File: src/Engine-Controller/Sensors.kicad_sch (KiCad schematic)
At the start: 24 parts, among them P10 39299043, P11 39299043, P12 39299043, P13 39299043, P14 39299043, P15 39299043, P8 39299043, P9 39299043, U12 MAX4617EUE+T, U13 MAX4617EUE+T, U7 MC74HC4066ADG, U8 AD623ARZ-R7, U9 MC74HC4066ADG

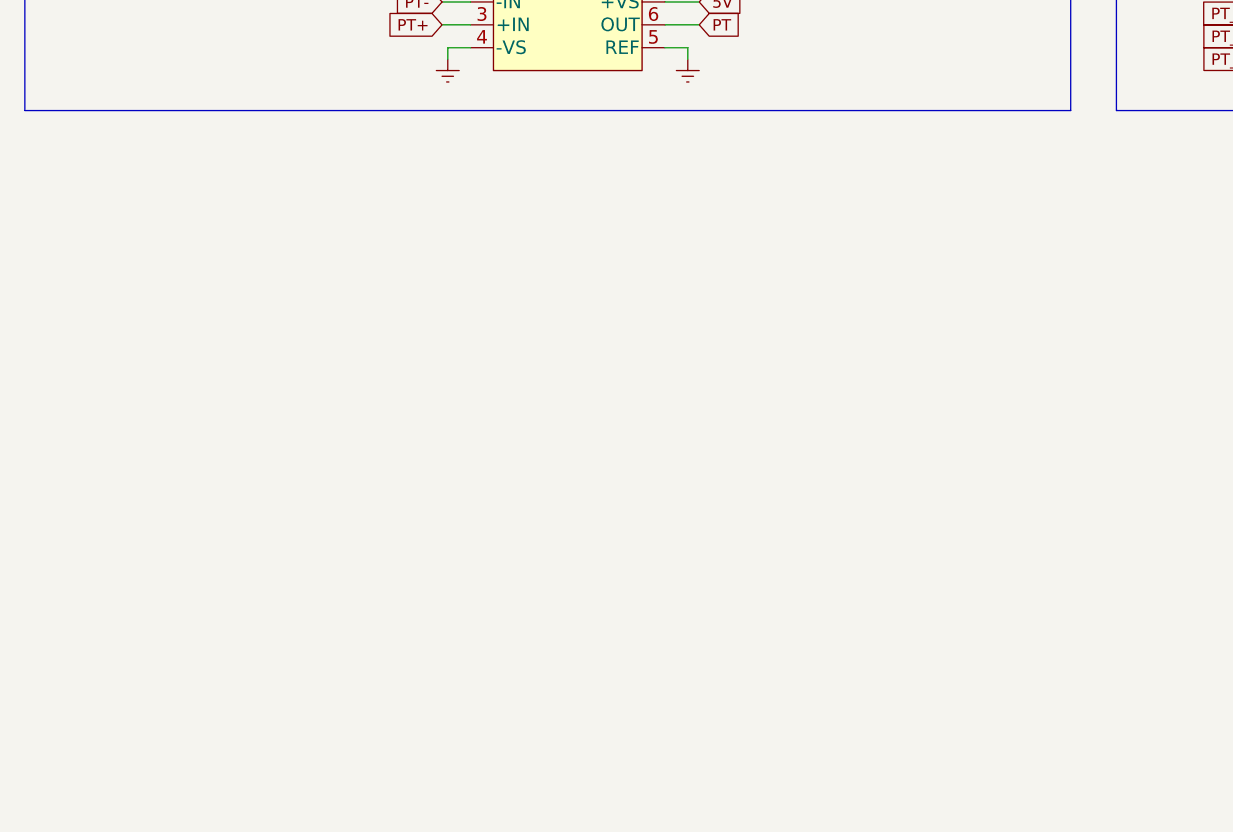
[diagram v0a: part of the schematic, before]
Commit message: added thermocouple IC to schematic
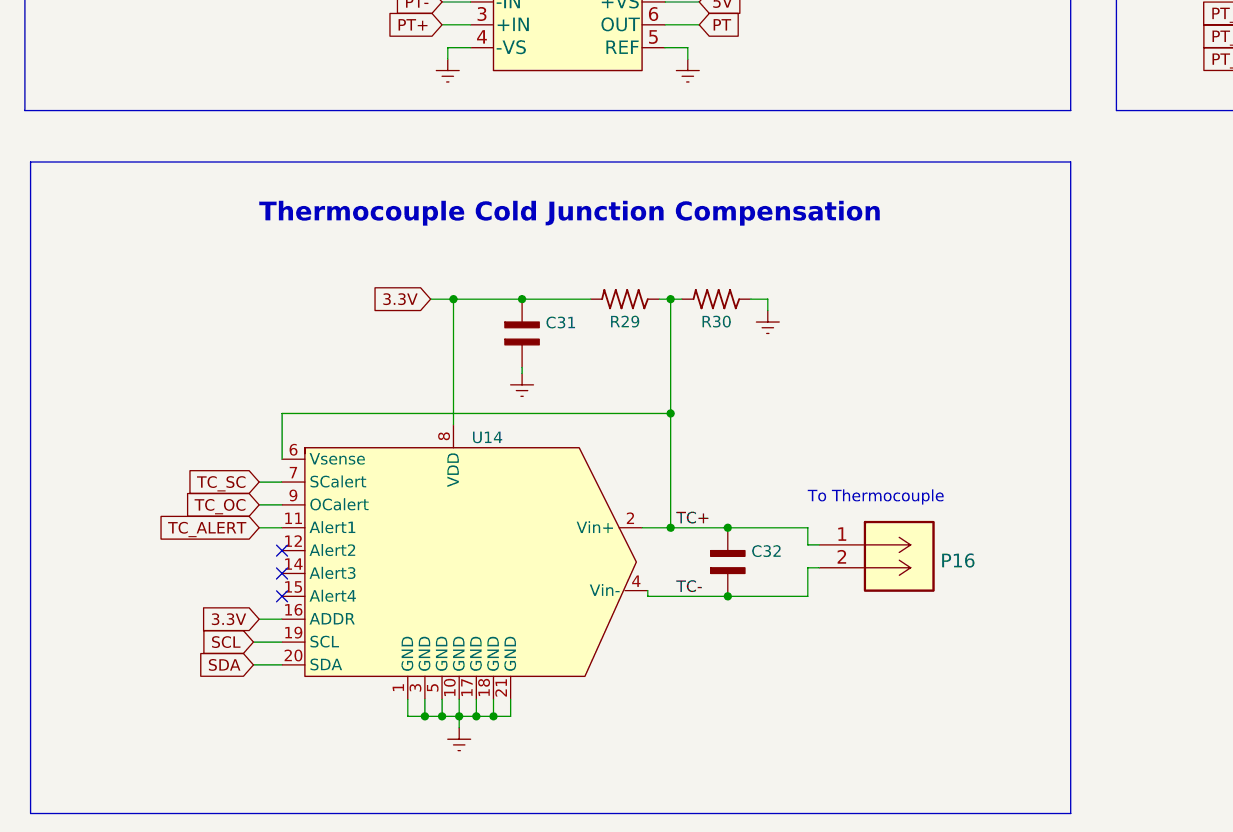
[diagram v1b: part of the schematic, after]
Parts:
- added C31, C32: (no value), symbol Engine-Controller:CAP_0603
- added P16: (no value), symbol Engine-Controller:647676-2
- added R29, R30: (no value), symbol Engine-Controller:RES_0603
- added U14: (no value), symbol Engine-Controller:MCP96L01T-E_MX
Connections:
- net 3.3V: now also C31.2, R29.2, U14.16 (ADDR), U14.8 (VDD)
- net Earth: now also C31.1, R30.1, U14.1 (GND), U14.10 (GND), U14.17 (GND), U14.18 (GND), U14.21 (GND), U14.3 (GND), U14.5 (GND)
- new net SCL: U14.19 (SCL)
- new net SDA: U14.20 (SDA)
- new net TC+: C32.2, P16.1, R29.1, R30.2, U14.2 (Vin+), U14.6 (Vsense)
- new net TC-: C32.1, P16.2, U14.4 (Vin-)
- new net TC_ALERT: U14.11 (Alert1)
- new net TC_OC: U14.9 (OCalert)
- new net TC_SC: U14.7 (SCalert)
- no-connect marks 0 -> 3
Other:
- note added: "Thermocouple Cold Junction Compensation"
- note added: "To Thermocouple"

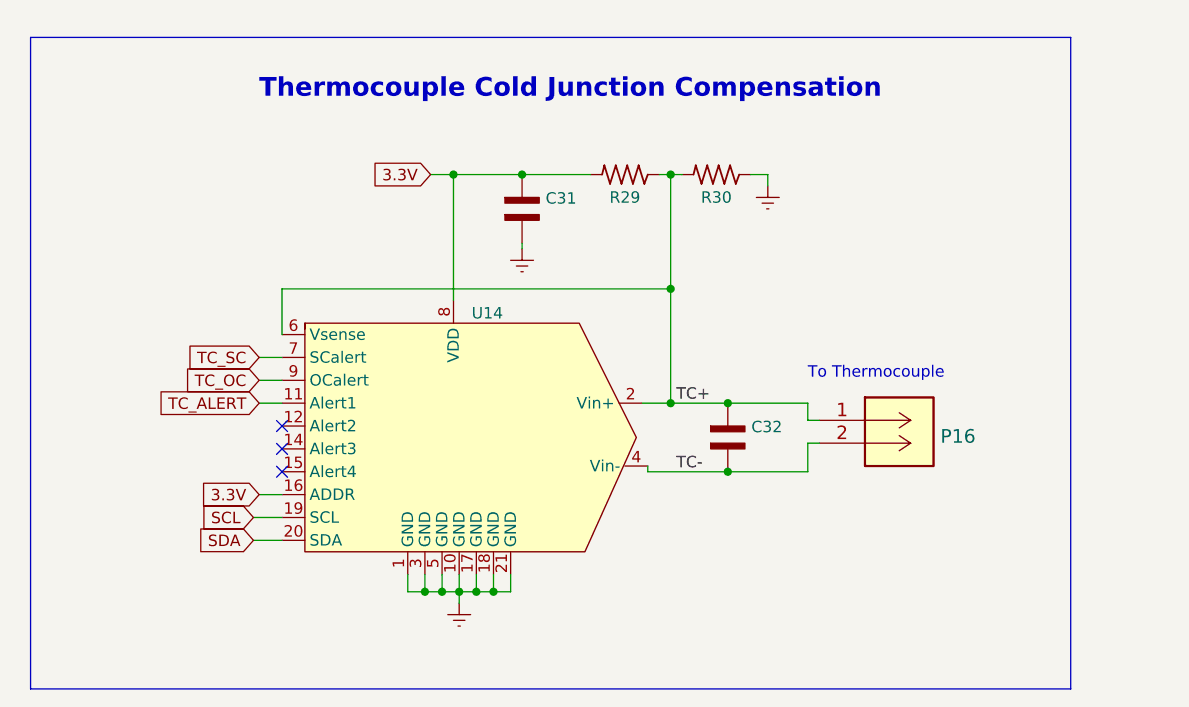
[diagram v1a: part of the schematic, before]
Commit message: added I2C pullups to thermocouple IC
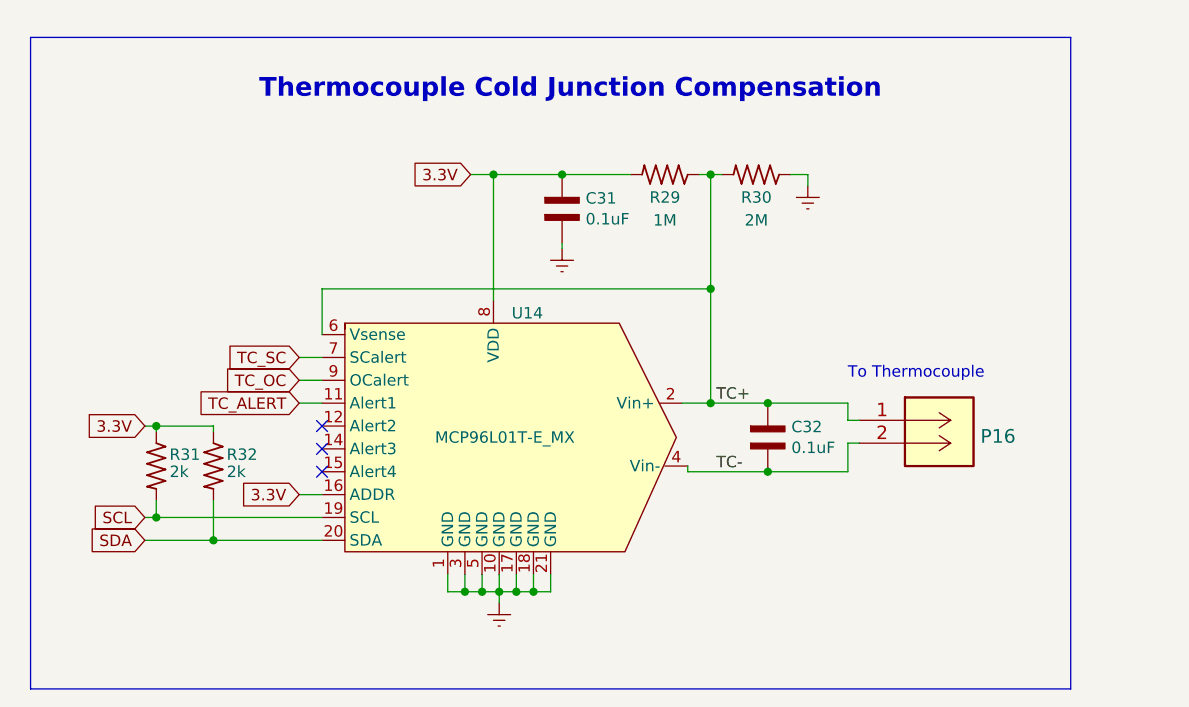
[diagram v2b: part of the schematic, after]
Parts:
- added R31, R32: 2k, symbol Engine-Controller:RES_0603
- C31: value (none) -> 0.1uF; footprint (none) -> Engine-Controller:CAP_0603
- C32: value (none) -> 0.1uF
- P16: value (none) -> 647676-2; footprint (none) -> CONN_2043-1X04G00DAU_OUP
- R29: value (none) -> 1M
- R30: value (none) -> 2M
- U14: value (none) -> MCP96L01T-E_MX
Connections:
- net 3.3V: now also R31.1, R32.1
- net SCL: now also R31.2
- net SDA: now also R32.2
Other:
- moved on the sheet: C31, C32, P16, R29, R30, U14

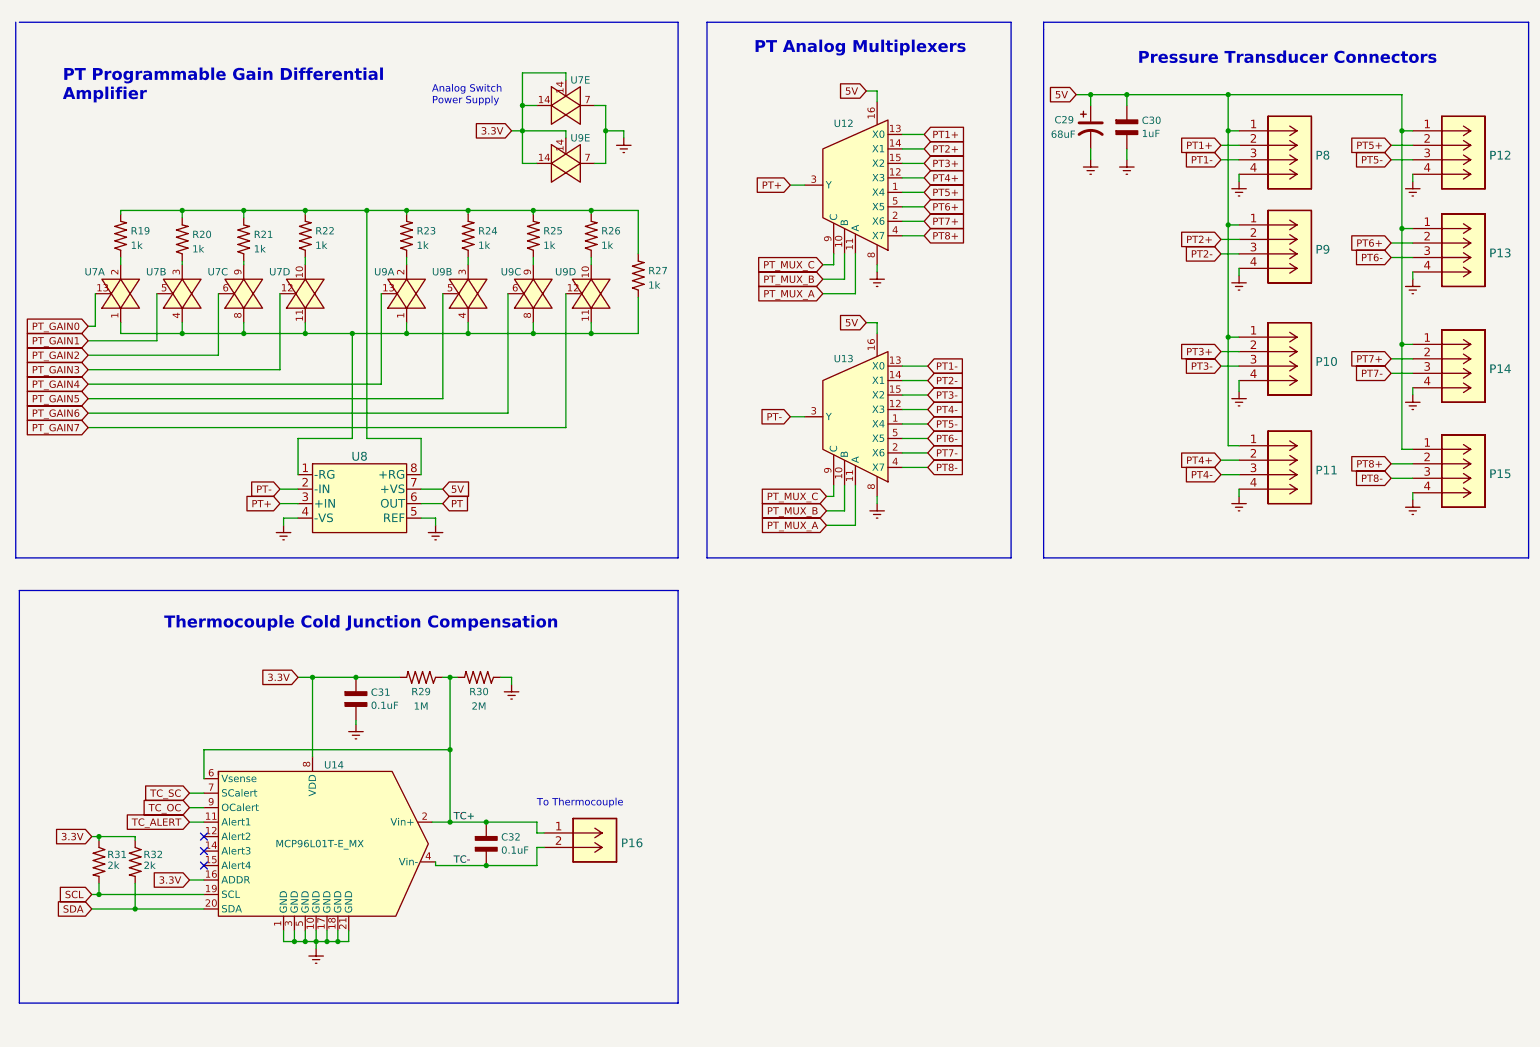
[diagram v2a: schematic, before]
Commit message: added load cell amplifier to schematic
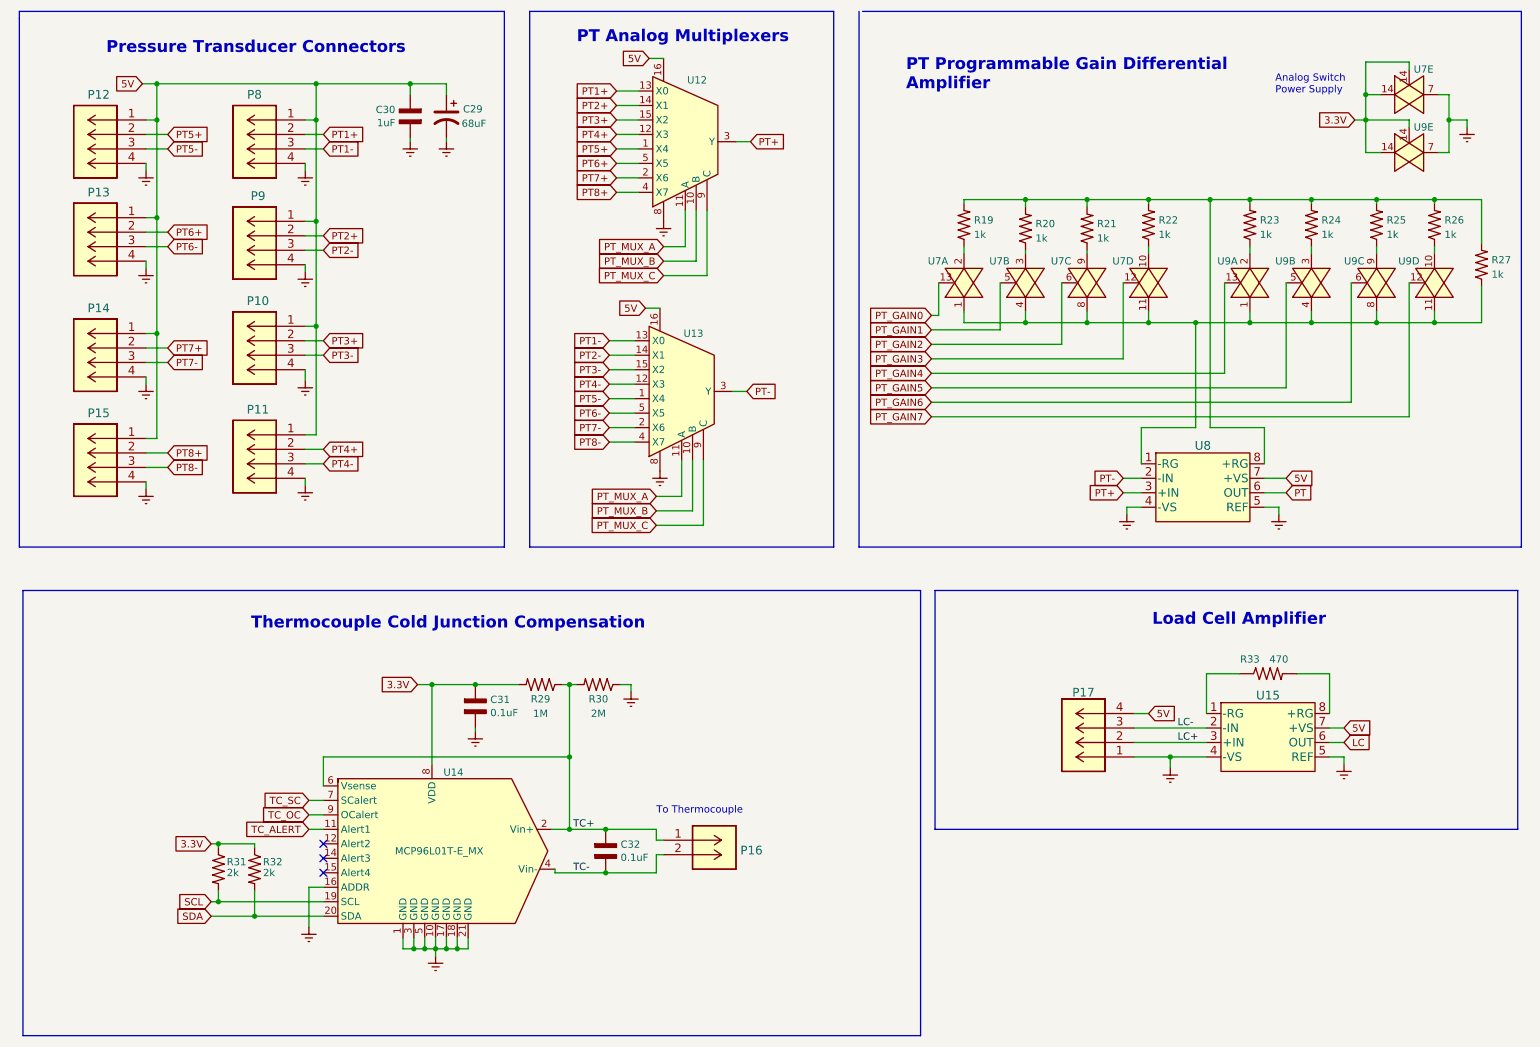
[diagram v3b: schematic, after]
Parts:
- added P17: 0530470410, CONN_4840.2201_SCH, symbol Engine-Controller:0530470410
- added R33: 470, symbol Engine-Controller:RES_0805
- added U15: AD623ARZ-R7, R_8_ADI, symbol Engine-Controller:AD623ARZ-R7
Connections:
- net 3.3V: no longer U14.16 (ADDR)
- net 5V: now also P17.4, U15.7 (+VS)
- net Earth: now also U14.16 (ADDR), P17.1 (+12V), U15.4 (-VS), U15.5 (REF)
- new net: R33.1, U15.1 (-RG)
- new net: R33.2, U15.8 (+RG)
- new net LC: U15.6 (OUT)
- new net LC+: P17.2 (GND), U15.3 (+IN)
- new net LC-: P17.3, U15.2 (-IN)
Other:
- note added: "Load Cell Amplifier"
- moved on the sheet: C29, C30, C31, C32, P10, P11, P12, P13, P14, P15, P16, P8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

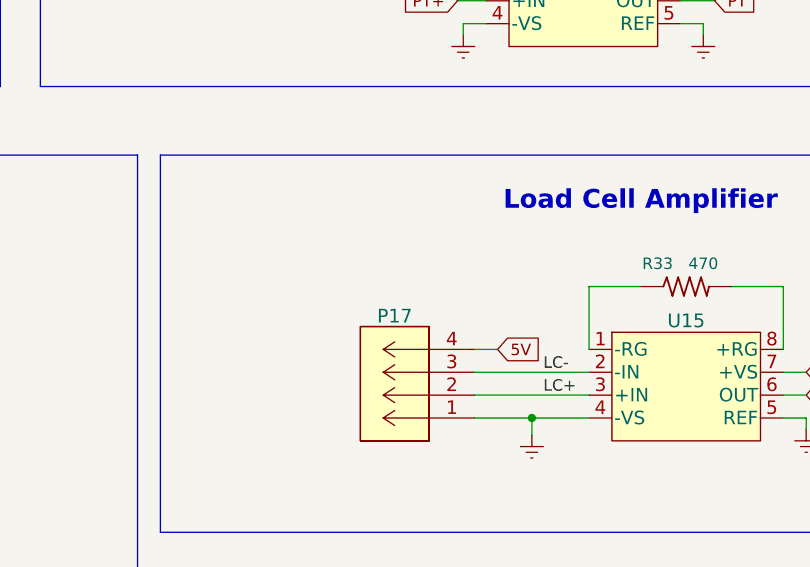
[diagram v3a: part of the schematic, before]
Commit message: added label to load cell connector
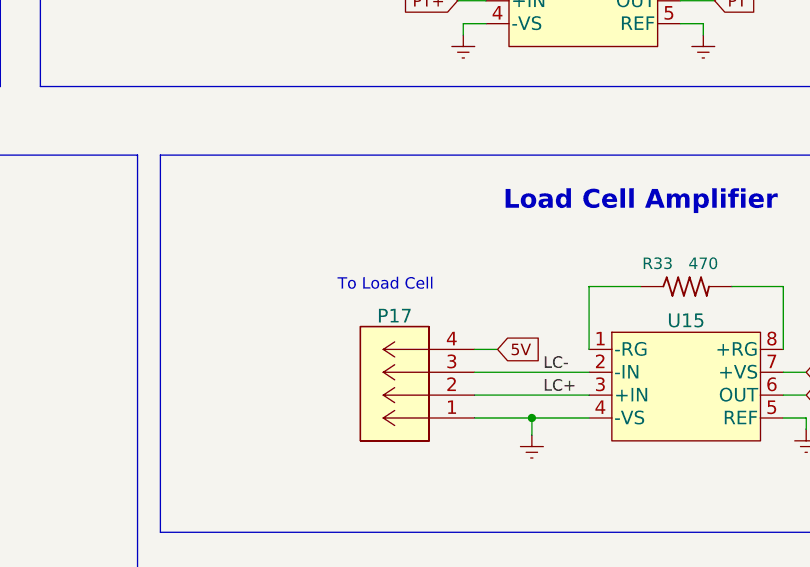
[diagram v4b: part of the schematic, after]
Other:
- note added: "To Load Cell"
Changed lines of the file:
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@@
     (effects (font (size 2.0828 2.0828) (thickness 0.4166) bold) (justify left bottom))
+  )
+  (text "To Load Cell" (at 196.215 132.715 0)
+    (effects (font (size 1.27 1.27)) (justify left bottom))
   )
   (text "Analog Switch \nPower Supply" (at 236.22 30.48 0)
